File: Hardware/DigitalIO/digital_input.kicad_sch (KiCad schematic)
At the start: 72 parts, among them Q2 PMOS, Q3 PMOS, Q4 PMOS, Q5 PMOS, Q6 PMOS, Q7 PMOS, Q8 PMOS, Q9 PMOS, U10 CNY17-1, U11 CNY17-1, U12 CNY17-1, U13 CNY17-1, U6 CNY17-1, U7 CNY17-1, U8 CNY17-1, U9 CNY17-1

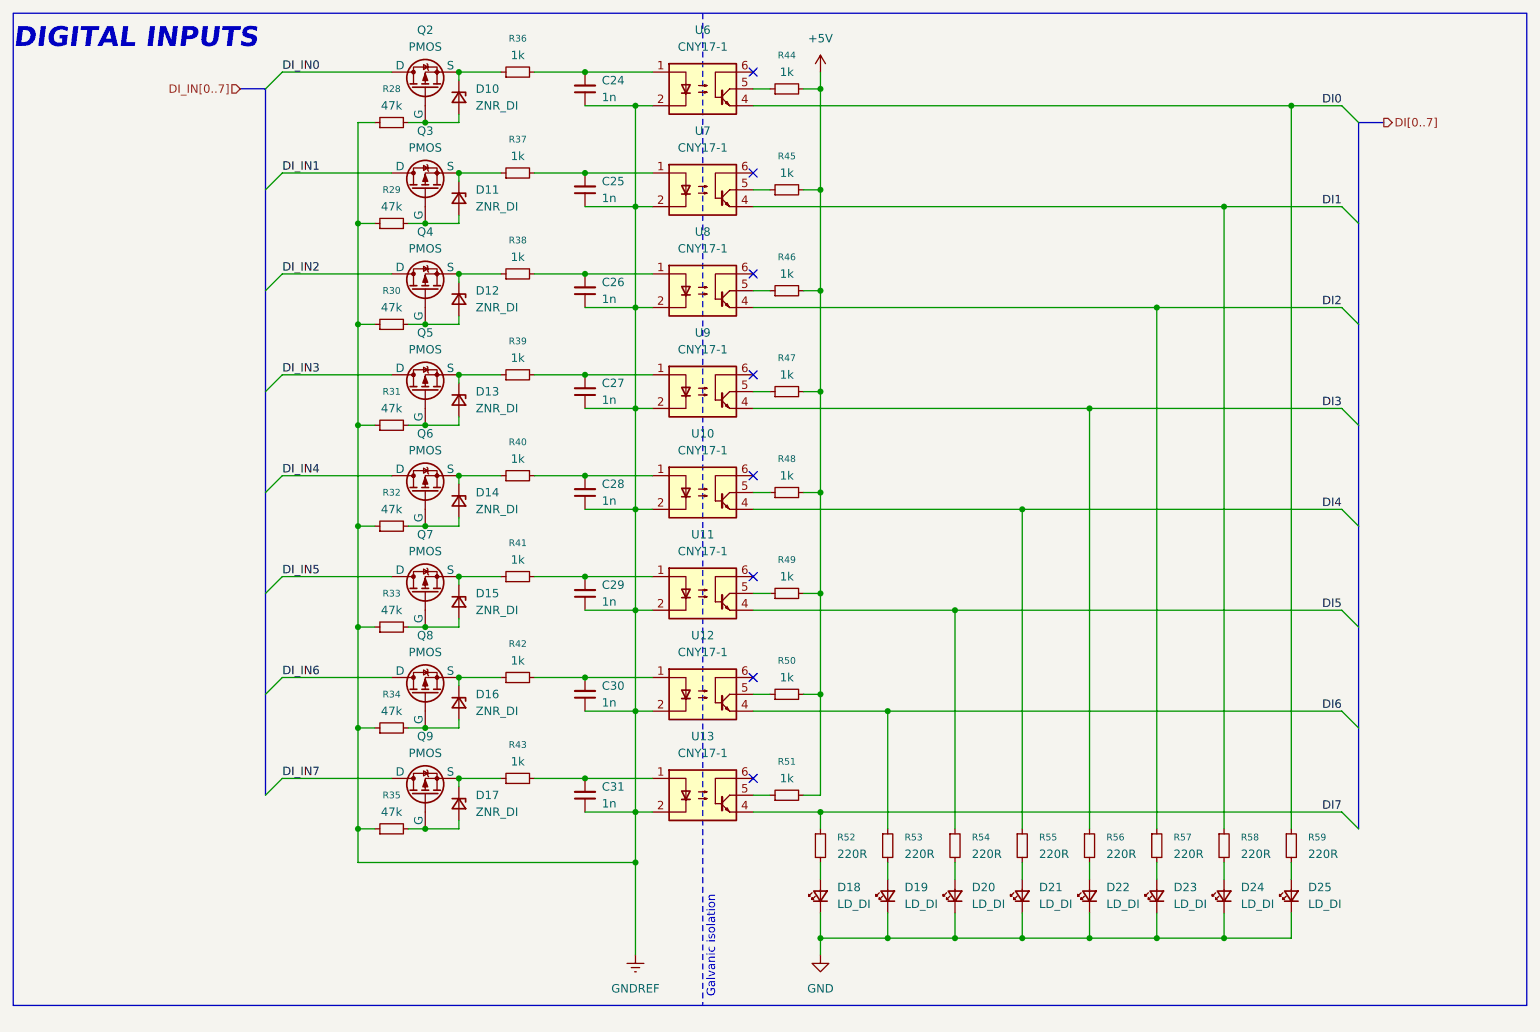
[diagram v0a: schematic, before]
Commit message: schematic update - all pcbs
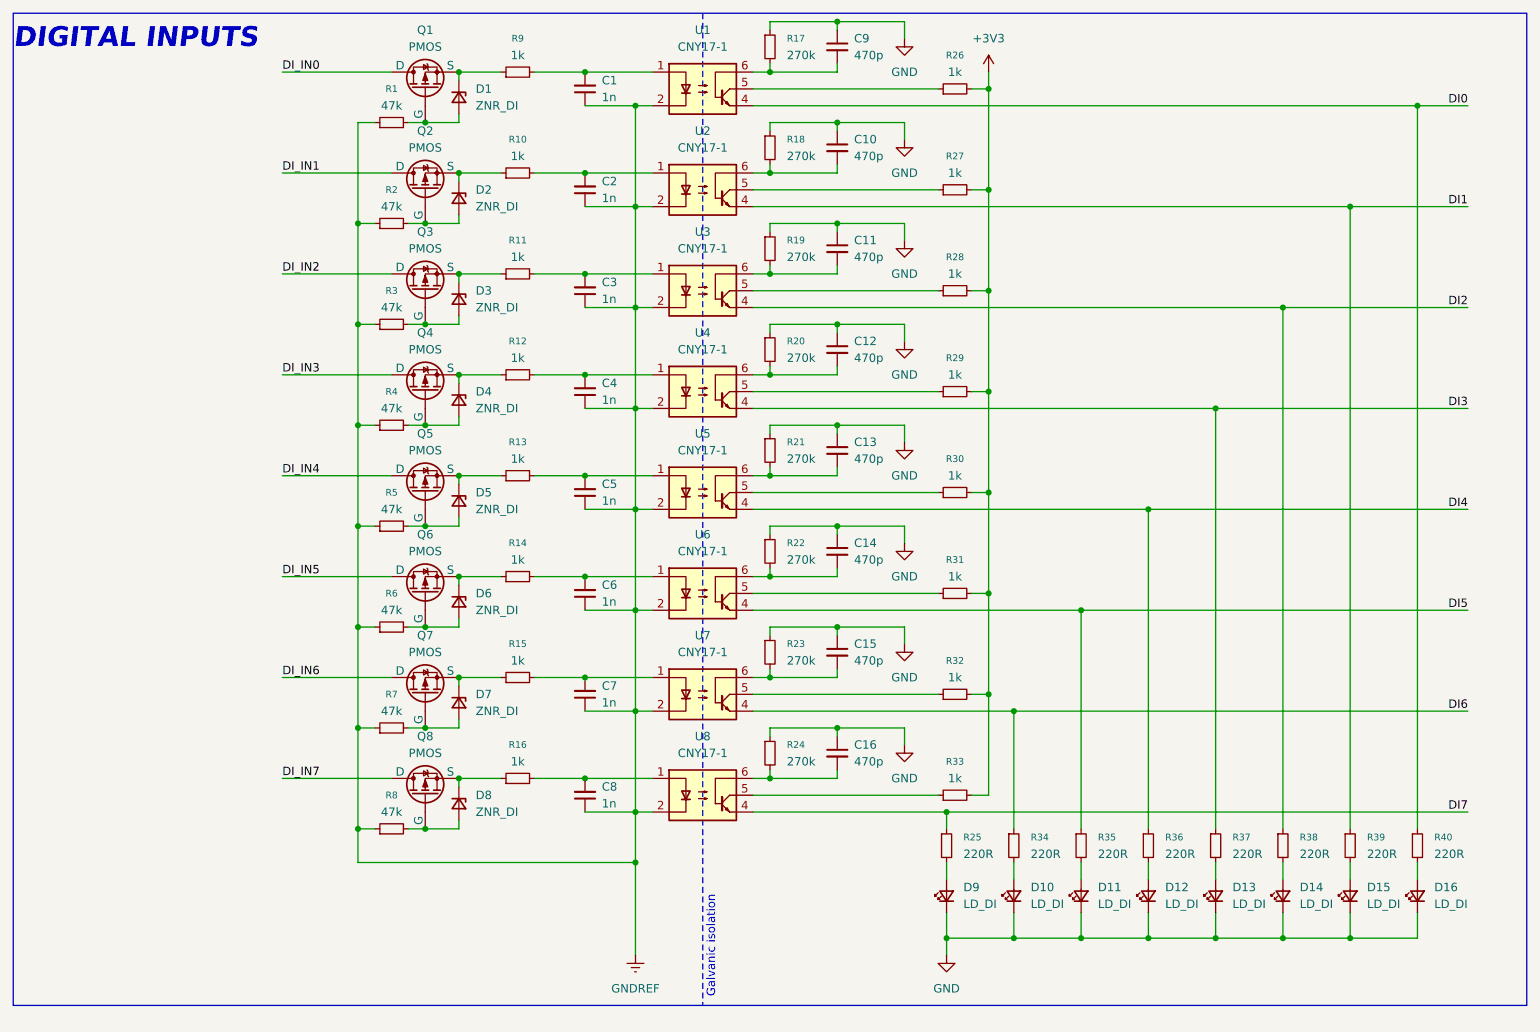
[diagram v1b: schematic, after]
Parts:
- added C10, C11, C12, C13, C14, C15, C16, C9: 470p, symbol Device:C_Small
- added R17, R18, R19, R20, R21, R22, R23, R24: 270k, symbol Device:R_Small
- D10: renamed from D19; footprint (none) -> LED_SMD:LED_0603_1608Metric_Pad1.05x0.95mm_HandSolder
- D11: renamed from D20; footprint (none) -> LED_SMD:LED_0603_1608Metric_Pad1.05x0.95mm_HandSolder
- D12: renamed from D21; footprint (none) -> LED_SMD:LED_0603_1608Metric_Pad1.05x0.95mm_HandSolder
- D13: renamed from D22; footprint (none) -> LED_SMD:LED_0603_1608Metric_Pad1.05x0.95mm_HandSolder
- D14: renamed from D23; footprint (none) -> LED_SMD:LED_0603_1608Metric_Pad1.05x0.95mm_HandSolder
- D15: renamed from D24; footprint (none) -> LED_SMD:LED_0603_1608Metric_Pad1.05x0.95mm_HandSolder
- D16: renamed from D25; footprint (none) -> LED_SMD:LED_0603_1608Metric_Pad1.05x0.95mm_HandSolder
- D9: renamed from D18; footprint (none) -> LED_SMD:LED_0603_1608Metric_Pad1.05x0.95mm_HandSolder
- renumbered C24 to C1, C25 to C2, C26 to C3, C27 to C4, C28 to C5, C29 to C6, C30 to C7, C31 to C8, D10 to D1, D11 to D2, D12 to D3, D13 to D4, D14 to D5, D15 to D6, D16 to D7, D17 to D8, Q2 to Q1, Q3 to Q2, Q4 to Q3, Q5 to Q4, Q6 to Q5, Q7 to Q6, Q8 to Q7, Q9 to Q8, R28 to R1, R37 to R10, R38 to R11, R39 to R12, R40 to R13, R41 to R14, R42 to R15, R43 to R16, R29 to R2, R52 to R25, R44 to R26, R45 to R27, R46 to R28, R47 to R29, R30 to R3, R48 to R30, R49 to R31, R50 to R32, R51 to R33, R53 to R34, R54 to R35, R55 to R36, R56 to R37, R57 to R38, R58 to R39, R31 to R4, R59 to R40, R32 to R5, R33 to R6, R34 to R7, R35 to R8, R36 to R9, U6 to U1, U7 to U2, U8 to U3, U9 to U4, U10 to U5, U11 to U6, U12 to U7, U13 to U8
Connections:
- net GND: now also C10.1, C11.1, C12.1, C13.1, C14.1, C15.1, C16.1, C9.1, R17.1, R18.1, R19.1, R20.1, R21.1, R22.1, R23.1, R24.1
- net at U3.6: now also C11.2, R19.2
- net at U5.6: now also C13.2, R21.2
- net at U6.6: now also C14.2, R22.2
- net at U4.6: now also C12.2, R20.2
- net at U8.6: now also C16.2, R24.2
- net at U2.6: now also C10.2, R18.2
- net at U1.6: now also C9.2, R17.2
- net at U7.6: now also C15.2, R23.2
- net +5V renamed +3V3
- no-connect marks 8 -> 0
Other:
- moved on the sheet: D10, D11, D12, D13, D14, D15, D16, D9, R25, R26, R27, R28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

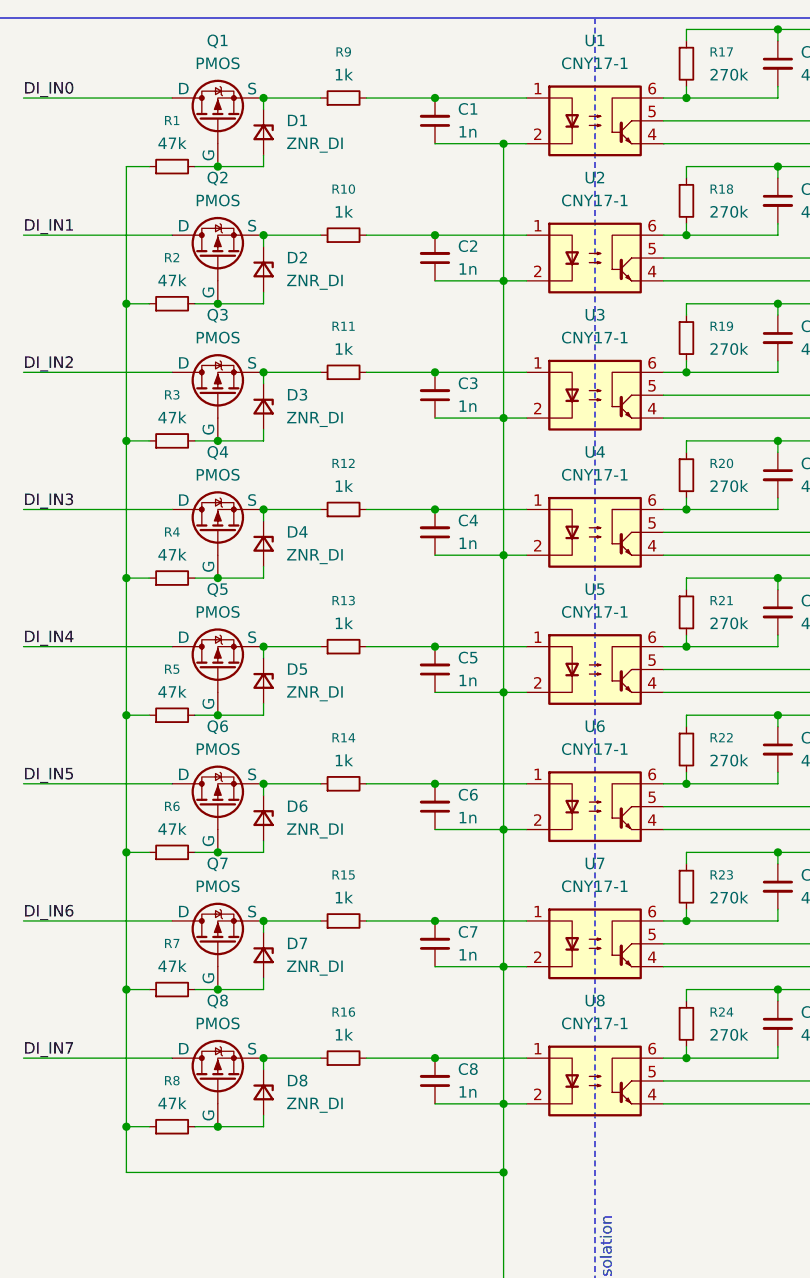
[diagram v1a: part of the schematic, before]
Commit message: schematic update - digital and analog footprints added
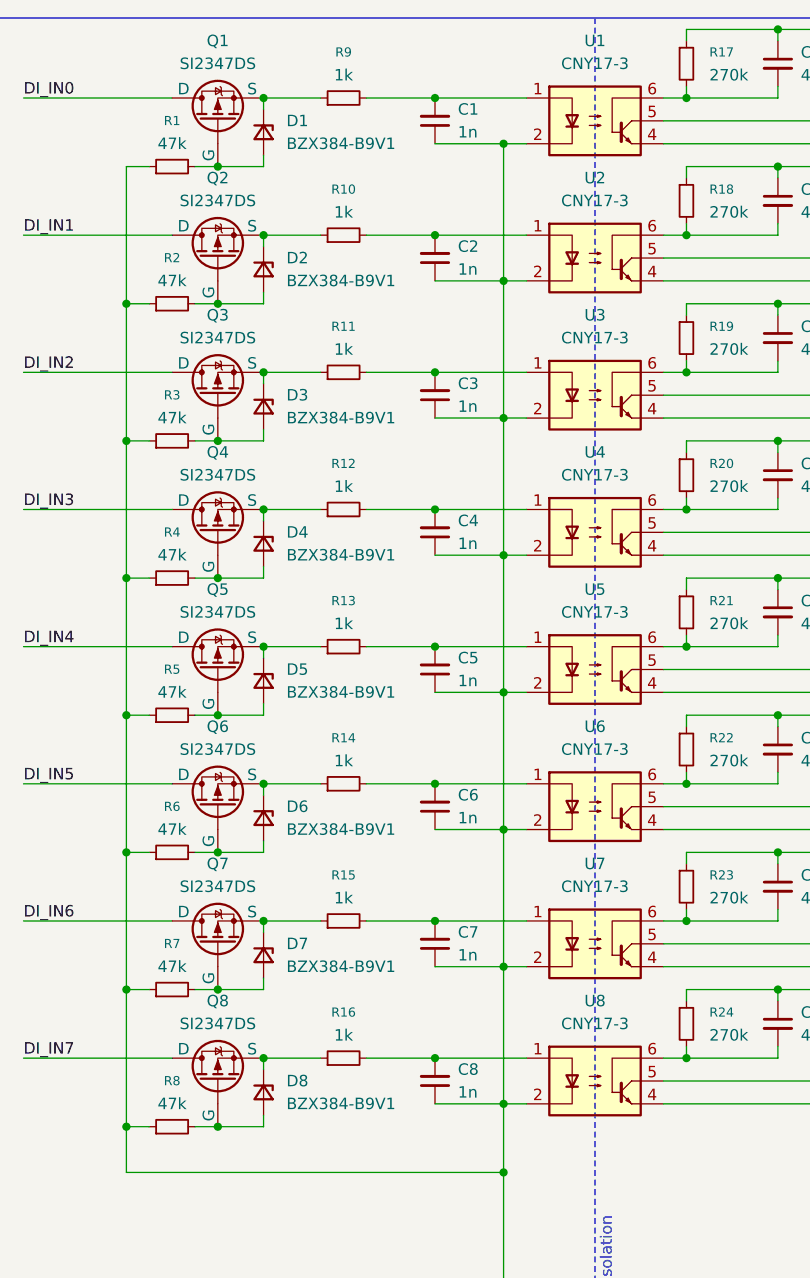
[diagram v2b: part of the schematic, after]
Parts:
- removed U1, U2, U3, U4, U5, U6, U7, U8: CNY17-1, symbol Isolator:CNY17-1
- added U1, U2, U3, U4, U5, U6, U7, U8: CNY17-3, PLC_STM:SOP254P1016X400-6N, symbol Isolator:CNY17-3
- C1, C2, C3, C4, C5, C6, C7, C8: footprint (none) -> Capacitor_SMD:C_0603_1608Metric_Pad1.08x0.95mm_HandSolder; Mouser Part Number (none) -> 81-GRT1885C1E102JA2D; Mouser Price/Stock (none) -> https://www.mouser.pl/ProductDetail/Murata-Electronics/GRT1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
- C10, C11, C12, C13, C14, C15, C16, C9: footprint (none) -> Capacitor_SMD:C_0603_1608Metric_Pad1.08x0.95mm_HandSolder; Mouser Part Number (none) -> 81-GRT188R71H471KE3D; Mouser Price/Stock (none) -> https://www.mouser.pl/ProductDetail/Murata-Electronics/GRT1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
- D1, D2, D3, D4, D5, D6, D7, D8: value ZNR_DI -> BZX384-B9V1; footprint (none) -> Diode_SMD:D_SOD-323_HandSoldering; Mouser Part Number (none) -> 771-BZX384-B9V1-T/R; Mouser Price/Stock (none) -> https://www.mouser.pl/ProductDetail/Nexperia/BZX384-B9V1115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
- Q1, Q2, Q3, Q4, Q5, Q6, Q7, Q8: value PMOS -> SI2347DS; footprint (none) -> Package_TO_SOT_SMD:SOT-23-3; Mouser Part Number (none) -> 78-SI2347DS-T1-GE3; Mouser Price/Stock (none) -> https://www.mouser.pl/ProductDetail/Vishay-Semiconductors/S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
- R1, R2, R3, R4, R5, R6, R7, R8: footprint (none) -> Resistor_SMD:R_0603_1608Metric_Pad0.98x0.95mm_HandSolder; Mouser Part Number (none) -> 71-CRCW0603-47K-E3; Mouser Price/Stock (none) -> https://www.mouser.pl/ProductDetail/Vishay/CRCW060347K0FKEA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
- R10, R11, R12, R13, R14, R15, R16, R26, R27, R28, R29, R30, R31, R32, R33, R9: footprint (none) -> Resistor_SMD:R_0603_1608Metric_Pad0.98x0.95mm_HandSolder; Mouser Part Number (none) -> 71-CRCW06031K00FKED; Mouser Price/Stock (none) -> https://www.mouser.pl/ProductDetail/Vishay/CRCW06031K00FKED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
- R17, R18, R19, R20, R21, R22, R23, R24: footprint (none) -> Resistor_SMD:R_0603_1608Metric_Pad0.98x0.95mm_HandSolder; Mouser Part Number (none) -> 71-CRCW0603-270K-E3; Mouser Price/Stock (none) -> https://www.mouser.pl/ProductDetail/Vishay/CRCW0603270KFKEA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
- R25, R34, R35, R36, R37, R38, R39, R40: footprint (none) -> Resistor_SMD:R_0603_1608Metric_Pad0.98x0.95mm_HandSolder; Mouser Part Number (none) -> 71-CRCW0603220RFKEAH; Mouser Price/Stock (none) -> https://www.mouser.pl/ProductDetail/Vishay/CRCW0603220RFKEA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
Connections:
- net DI0: now also U1.4
- net DI1: now also U2.4
- net DI2: now also U3.4
- net DI3: now also U4.4
- net DI4: now also U5.4
- net DI5: now also U6.4
- net DI6: now also U7.4
- net DI7: now also U8.4
- net GNDREF: now also U1.2, U2.2, U3.2, U4.2, U5.2, U6.2, U7.2, U8.2
- net at C4.2, R12.2: now also U4.1
- net at C5.2, R13.2: now also U5.1
- net at C15.2, R23.2: now also U7.6
- net at C8.2, R16.2: now also U8.1
- net at C3.2, R11.2: now also U3.1
- net at C7.2, R15.2: now also U7.1
- net at R28.1: now also U3.5
- net at C11.2, R19.2: now also U3.6
- net at R30.1: now also U5.5
- net at C13.2, R21.2: now also U5.6
- net at C14.2, R22.2: now also U6.6
- net at C6.2, R14.2: now also U6.1
- net at R31.1: now also U6.5
- net at C10.2, R18.2: now also U2.6
- net at R29.1: now also U4.5
- net at C12.2, R20.2: now also U4.6
- net at C9.2, R17.2: now also U1.6
- net at R26.1: now also U1.5
- net at R32.1: now also U7.5
- net at C2.2, R10.2: now also U2.1
- net at R33.1: now also U8.5
- net at C16.2, R24.2: now also U8.6
- net at C1.2, R9.2: now also U1.1
- net at R27.1: now also U2.5
